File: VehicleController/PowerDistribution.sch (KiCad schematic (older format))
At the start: 20 parts, among them U10 BTS6133D, U11 R-78E5.0-1.0, U9 TL431

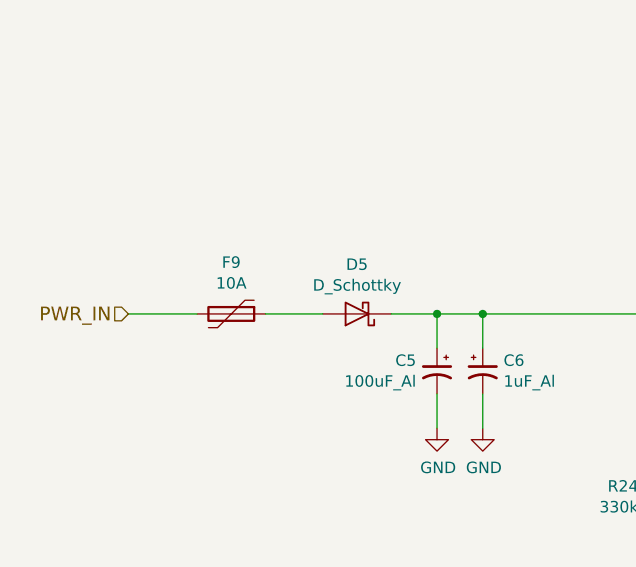
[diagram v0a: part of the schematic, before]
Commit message: Re-do MX120, GDS->GSD, Associations.
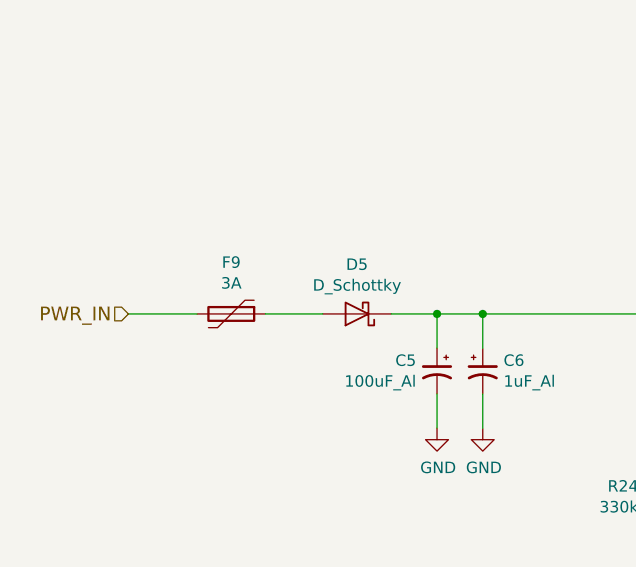
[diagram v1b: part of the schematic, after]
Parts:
- C6: footprint Capacitors_SMD:c_elec_4x4.5 -> Capacitors_SMD:C_0805_HandSoldering
- D5, D6: footprint Diodes_SMD:SMA_Handsoldering -> Diodes_SMD:D_SMC_Handsoldering
- D7: footprint (none) -> Diodes_SMD:D_SOD-323_HandSoldering
- F10: footprint Fuse_Holders_and_Fuses:Fuse_SMD1206_HandSoldering -> Resistors_SMD:R_1210_HandSoldering
- F9: value 10A -> 3A; footprint (none) -> Resistors_SMD:R_1210_HandSoldering
- U10: footprint UNCAMotorsports:TO-252-5 -> UNCA Motorsports:TO-252-5
- U11: footprint UNCAMotorsports:R-78Cxx-1.0 -> UNCA Motorsports:R-78Cxx-1.0
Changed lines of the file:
@@
 F 0 "D5" H 3000 2534 50  0000 C CNN
 F 1 "D_Schottky" H 3000 2625 50  0000 C CNN
-F 2 "Diodes_SMD:SMA_Handsoldering" H 3000 2750 50  0001 C CNN
+F 2 "Diodes_SMD:D_SMC_Handsoldering" H 3000 2750 50  0001 C CNN
 F 3 "" H 3000 2750 50  0000 C CNN
 	1    3000 2750
@@
 P 2450 2750
 F 0 "F9" V 2225 2750 50  0000 C CNN
-F 1 "10A" V 2316 2750 50  0000 C CNN
-F 2 "" H 2500 2550 50  0001 L CNN
+F 1 "3A" V 2316 2750 50  0000 C CNN
+F 2 "Resistors_SMD:R_1210_HandSoldering" H 2500 2550 50  0001 L CNN
 F 3 "" H 2450 2750 50  0001 C CNN
 	1    2450 2750
@@
 F 0 "U10" H 6550 3237 60  0000 C CNN
 F 1 "BTS6133D" H 6550 3131 60  0000 C CNN
-F 2 "UNCAMotorsports:TO-252-5" H 6700 3050 60  0001 C CNN
+F 2 "UNCA Motorsports:TO-252-5" H 6700 3050 60  0001 C CNN
 F 3 "" H 6700 3050 60  0000 C CNN
 	1    6550 2850
@@
 $EndComp
 $Comp
-L GND #PWR43
+L GND #PWR042
 U 1 1 587C7BE3
 P 5850 3650
-F 0 "#PWR43" H 5850 3400 50  0001 C CNN
+F 0 "#PWR042" H 5850 3400 50  0001 C CNN
 F 1 "GND" H 5855 3477 50  0000 C CNN
 F 2 "" H 5850 3650 50  0000 C CNN
@@
 $EndComp
 $Comp
-L GND #PWR42
+L GND #PWR043
 U 1 1 587C7BF7
 P 4300 4700
-F 0 "#PWR42" H 4300 4450 50  0001 C CNN
+F 0 "#PWR043" H 4300 4450 50  0001 C CNN
 F 1 "GND" H 4305 4527 50  0000 C CNN
 F 2 "" H 4300 4700 50  0000 C CNN
@@
 $EndComp
 $Comp
-L GND #PWR45
+L GND #PWR044
 U 1 1 58AEB860
 P 8650 3250
-F 0 "#PWR45" H 8650 3000 50  0001 C CNN
+F 0 "#PWR044" H 8650 3000 50  0001 C CNN
 F 1 "GND" H 8655 3077 50  0000 C CNN
 F 2 "" H 8650 3250 50  0000 C CNN
@@
 5V
 $Comp
-L PWR_FLAG #FLG3
+L PWR_FLAG #FLG045
 U 1 1 58AF2028
 P 5550 1000
-F 0 "#FLG3" H 5550 1095 50  0001 C CNN
+F 0 "#FLG045" H 5550 1095 50  0001 C CNN
 F 1 "PWR_FLAG" H 5550 1224 50  0001 C CNN
 F 2 "" H 5550 1000 50  0000 C CNN
@@
 12V
 $Comp
-L GND #PWR40
+L GND #PWR046
 U 1 1 58B0EFE3
 P 3350 3250
-F 0 "#PWR40" H 3350 3000 50  0001 C CNN
+F 0 "#PWR046" H 3350 3000 50  0001 C CNN
 F 1 "GND" H 3355 3077 50  0000 C CNN
 F 2 "" H 3350 3250 50  0000 C CNN
@@
 $EndComp
 $Comp
-L GND #PWR41
+L GND #PWR047
 U 1 1 58B0F09D
 P 3550 3250
-F 0 "#PWR41" H 3550 3000 50  0001 C CNN
+F 0 "#PWR047" H 3550 3000 50  0001 C CNN
 F 1 "GND" H 3555 3077 50  0000 C CNN
 F 2 "" H 3550 3250 50  0000 C CNN
@@
 F 0 "D6" V 5354 3929 50  0000 L CNN
 F 1 "D_ALT" V 5445 3929 50  0000 L CNN
-F 2 "Diodes_SMD:SMA_Handsoldering" H 5400 3850 50  0001 C CNN
+F 2 "Diodes_SMD:D_SMC_Handsoldering" H 5400 3850 50  0001 C CNN
 F 3 "" H 5400 3850 50  0000 C CNN
 	1    5400 3850
@@
 $EndComp
 $Comp
-L +5V #PWR47
+L +5V #PWR048
 U 1 1 58BE7A1A
 P 9300 2600
-F 0 "#PWR47" H 9350 2650 50  0001 C CNN
+F 0 "#PWR048" H 9350 2650 50  0001 C CNN
 F 1 "+5V" H 9315 2773 50  0000 C CNN
 F 2 "" H 550 -100 50  0001 C CNN
@@
 F 0 "F10" V 7625 2750 50  0000 C CNN
 F 1 "1A" V 7716 2750 50  0000 C CNN
-F 2 "Fuse_Holders_and_Fuses:Fuse_SMD1206_HandSoldering" H 7900 2550 50  0001 L CNN
+F 2 "Resistors_SMD:R_1210_HandSoldering" H 7900 2550 50  0001 L CNN
 F 3 "" H 7850 2750 50  0001 C CNN
 	1    7850 2750
@@
 $EndComp
 $Comp
-L GND #PWR44
+L GND #PWR049
 U 1 1 58C31B60
 P 7500 3500
-F 0 "#PWR44" H 7500 3250 50  0001 C CNN
+F 0 "#PWR049" H 7500 3250 50  0001 C CNN
 F 1 "GND" H 7505 3327 50  0000 C CNN
 F 2 "" H 7500 3500 50  0000 C CNN
@@
 $EndComp
 $Comp
-L GND #PWR48
+L GND #PWR050
 U 1 1 58C32364
 P 9650 3500
-F 0 "#PWR48" H 9650 3250 50  0001 C CNN
+F 0 "#PWR050" H 9650 3250 50  0001 C CNN
 F 1 "GND" H 9655 3327 50  0000 C CNN
 F 2 "" H 9650 3500 50  0000 C CNN
@@
 F 0 "C6" H 3641 3046 50  0000 L CNN
 F 1 "1uF_Al" H 3641 2955 50  0000 L CNN
-F 2 "Capacitors_SMD:c_elec_4x4.5" H 900 -350 50  0001 C CNN
+F 2 "Capacitors_SMD:C_0805_HandSoldering" H 900 -350 50  0001 C CNN
 F 3 "" H 900 -350 50  0001 C CNN
 	1    3550 3000
@@
 F 0 "U11" H 8650 3037 60  0000 C CNN
 F 1 "R-78E5.0-1.0" H 8650 2931 60  0000 C CNN
-F 2 "UNCAMotorsports:R-78Cxx-1.0" H 2600 1150 60  0001 C CNN
+F 2 "UNCA Motorsports:R-78Cxx-1.0" H 2600 1150 60  0001 C CNN
 F 3 "" H 2600 1150 60  0000 C CNN
 	1    8650 2750
@@
 F 0 "D7" H 6050 3390 50  0000 C CNN
 F 1 "3.3V" H 6050 3210 50  0000 C CNN
-F 2 "" V 6050 3300 50  0001 C CNN
+F 2 "Diodes_SMD:D_SOD-323_HandSoldering" V 6050 3300 50  0001 C CNN
 F 3 "" V 6050 3300 50  0001 C CNN
 	1    6050 3300

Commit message: Library Fixes
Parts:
- D5, D6: footprint Diodes_SMD:D_SMC_Handsoldering -> Diodes_SMD:SMC_Handsoldering
- D7: footprint Diodes_SMD:D_SOD-323_HandSoldering -> Diodes_SMD:SOD-323
- U10: footprint UNCA Motorsports:TO-252-5 -> UNCAMotorsports:TO-252-5
- U11: footprint UNCA Motorsports:R-78Cxx-1.0 -> UNCAMotorsports:R-78Cxx-1.0
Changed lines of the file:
@@
 F 0 "D5" H 3000 2534 50  0000 C CNN
 F 1 "D_Schottky" H 3000 2625 50  0000 C CNN
-F 2 "Diodes_SMD:D_SMC_Handsoldering" H 3000 2750 50  0001 C CNN
+F 2 "Diodes_SMD:SMC_Handsoldering" H 3000 2750 50  0001 C CNN
 F 3 "" H 3000 2750 50  0000 C CNN
 	1    3000 2750
@@
 F 0 "U10" H 6550 3237 60  0000 C CNN
 F 1 "BTS6133D" H 6550 3131 60  0000 C CNN
-F 2 "UNCA Motorsports:TO-252-5" H 6700 3050 60  0001 C CNN
+F 2 "UNCAMotorsports:TO-252-5" H 6700 3050 60  0001 C CNN
 F 3 "" H 6700 3050 60  0000 C CNN
 	1    6550 2850
@@
 F 0 "D6" V 5354 3929 50  0000 L CNN
 F 1 "D_ALT" V 5445 3929 50  0000 L CNN
-F 2 "Diodes_SMD:D_SMC_Handsoldering" H 5400 3850 50  0001 C CNN
+F 2 "Diodes_SMD:SMC_Handsoldering" H 5400 3850 50  0001 C CNN
 F 3 "" H 5400 3850 50  0000 C CNN
 	1    5400 3850
@@
 F 0 "U11" H 8650 3037 60  0000 C CNN
 F 1 "R-78E5.0-1.0" H 8650 2931 60  0000 C CNN
-F 2 "UNCA Motorsports:R-78Cxx-1.0" H 2600 1150 60  0001 C CNN
+F 2 "UNCAMotorsports:R-78Cxx-1.0" H 2600 1150 60  0001 C CNN
 F 3 "" H 2600 1150 60  0000 C CNN
 	1    8650 2750
@@
 F 0 "D7" H 6050 3390 50  0000 C CNN
 F 1 "3.3V" H 6050 3210 50  0000 C CNN
-F 2 "Diodes_SMD:D_SOD-323_HandSoldering" V 6050 3300 50  0001 C CNN
+F 2 "Diodes_SMD:SOD-323" V 6050 3300 50  0001 C CNN
 F 3 "" V 6050 3300 50  0001 C CNN
 	1    6050 3300

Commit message: Small schematic fixes, start layout
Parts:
- D5, D6: footprint Diodes_SMD:SMC_Handsoldering -> Diodes_SMD:SMA_Handsoldering
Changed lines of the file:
@@
 LIBS:VehicleController-rescue
 LIBS:UNCAMotorsports
-LIBS:power
-LIBS:device
-LIBS:transistors
-LIBS:conn
-LIBS:linear
-LIBS:regul
-LIBS:74xx
-LIBS:cmos4000
-LIBS:adc-dac
-LIBS:memory
-LIBS:xilinx
-LIBS:microcontrollers
-LIBS:dsp
-LIBS:microchip
-LIBS:analog_switches
-LIBS:motorola
-LIBS:texas
-LIBS:intel
-LIBS:audio
-LIBS:interface
-LIBS:digital-audio
-LIBS:philips
-LIBS:display
-LIBS:cypress
-LIBS:siliconi
-LIBS:opto
-LIBS:atmel
-LIBS:contrib
-LIBS:valves
 LIBS:Common-Parts-Library-CPL
 LIBS:relays
 LIBS:SystemBlocks
-LIBS:dc-dc
-LIBS:Power_Management
-LIBS:switches
 LIBS:VehicleController-cache
-EELAYER 25 0
+EELAYER 26 0
 EELAYER END
 $Descr A4 11693 8268
@@
 F 0 "D5" H 3000 2534 50  0000 C CNN
 F 1 "D_Schottky" H 3000 2625 50  0000 C CNN
-F 2 "Diodes_SMD:SMC_Handsoldering" H 3000 2750 50  0001 C CNN
+F 2 "Diodes_SMD:SMA_Handsoldering" H 3000 2750 50  0001 C CNN
 F 3 "" H 3000 2750 50  0000 C CNN
 	1    3000 2750
@@
 F 0 "D6" V 5354 3929 50  0000 L CNN
 F 1 "D_ALT" V 5445 3929 50  0000 L CNN
-F 2 "Diodes_SMD:SMC_Handsoldering" H 5400 3850 50  0001 C CNN
+F 2 "Diodes_SMD:SMA_Handsoldering" H 5400 3850 50  0001 C CNN
 F 3 "" H 5400 3850 50  0000 C CNN
 	1    5400 3850

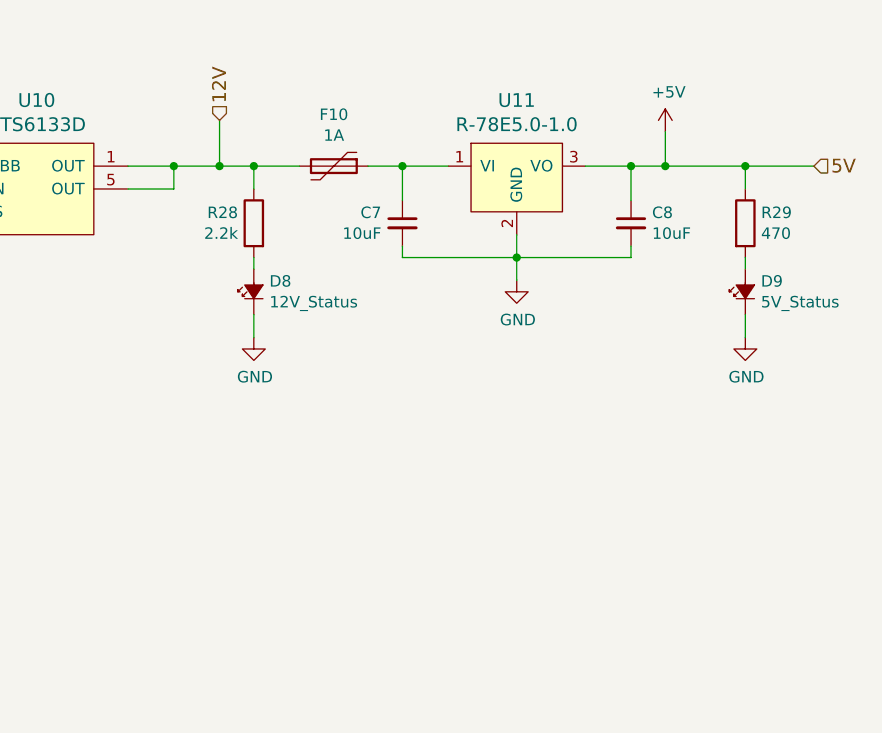
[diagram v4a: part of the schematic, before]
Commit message: 2x10 connector is now a nanofit, VCU
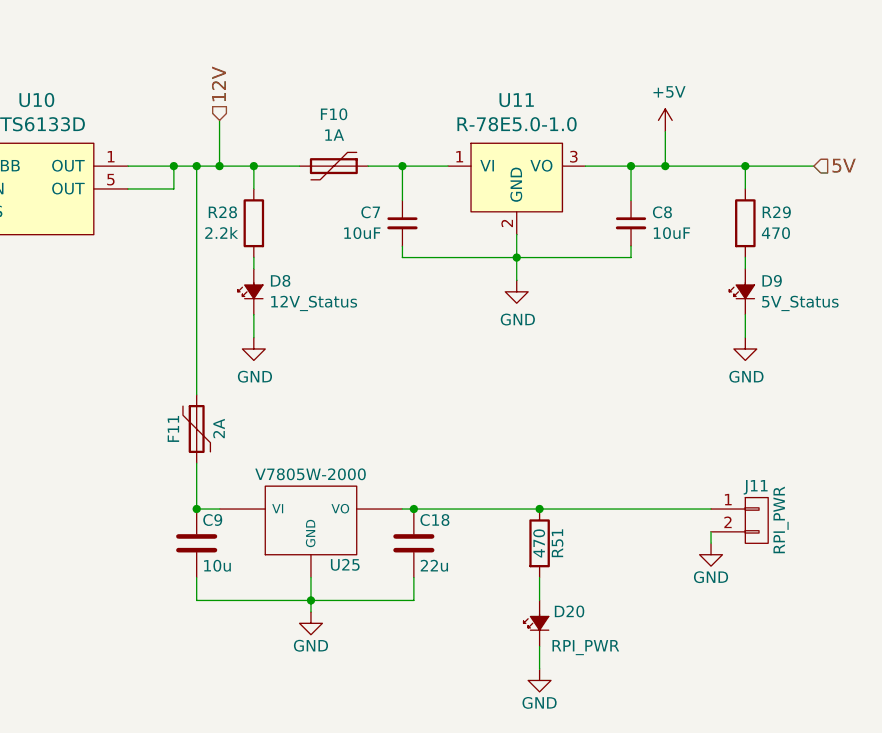
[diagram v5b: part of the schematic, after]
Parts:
- added C18: 22u, Capacitors_SMD:C_0805_HandSoldering, symbol C
- added C9: 10u, Capacitors_SMD:C_0805_HandSoldering, symbol C
- added D20: RPI_PWR, LEDs:LED_0805, symbol LED_Small_ALT
- added F11: 2A, Resistors_SMD:R_1210_HandSoldering, symbol Polyfuse
- added J11: RPI_PWR, Connectors_Molex:Molex_NanoFit_1x02x2.50mm_Straight, symbol CONN_01X02
- added R51: 470, Resistors_SMD:R_0805_HandSoldering, symbol R
- added U25: V7805W-2000, UNCAMotorsports:R-78Cxx-1.0, symbol V7805W-500
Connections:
- net 12V: now also F11.1
- net GND: now also C18.2, C9.2, D20.1 (K), J11.2 (P2), U25.2 (GND)
- new net: C9.1, F11.2, U25.1 (VI)
- new net: C18.1, J11.1 (P1), R51.1, U25.3 (VO)
- new net: D20.2 (A), R51.2
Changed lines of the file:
@@
 Wire Wire Line
 	6050 3550 5850 3550
+$Comp
+L V7805W-500 U25
+U 1 1 5930FD3A
+P 7750 4300
+F 0 "U25" H 7900 4104 50  0000 C CNN
+F 1 "V7805W-2000" H 7750 4500 50  0000 C CNN
+F 2 "UNCAMotorsports:R-78Cxx-1.0" H 7750 4300 50  0001 C CNN
+F 3 "" H 7750 4300 50  0000 C CNN
+	1    7750 4300
+	1    0    0    -1
+$EndComp
+Wire Wire Line
+	7250 4250 7350 4250
+Connection ~ 7250 2750
+$Comp
+L GND #PWR051
+U 1 1 5930FE1B
+P 7750 4700
+F 0 "#PWR051" H 7750 4450 50  0001 C CNN
+F 1 "GND" H 7750 4550 50  0000 C CNN
+F 2 "" H 7750 4700 50  0001 C CNN
+F 3 "" H 7750 4700 50  0001 C CNN
+	1    7750 4700
+	1    0    0    -1
+$EndComp
+Wire Wire Line
+	7750 4700 7750 4550
+$Comp
+L C C9
+U 1 1 5930FEB3
+P 7250 4400
+F 0 "C9" H 7275 4500 50  0000 L CNN
+F 1 "10u" H 7275 4300 50  0000 L CNN
+F 2 "Capacitors_SMD:C_0805_HandSoldering" H 7288 4250 50  0001 C CNN
+F 3 "" H 7250 4400 50  0001 C CNN
+	1    7250 4400
+	1    0    0    -1
+$EndComp
+$Comp
+L C C18
+U 1 1 5930FF1A
+P 8200 4400
+F 0 "C18" H 8225 4500 50  0000 L CNN
+F 1 "22u" H 8225 4300 50  0000 L CNN
+F 2 "Capacitors_SMD:C_0805_HandSoldering" H 8238 4250 50  0001 C CNN
+F 3 "" H 8200 4400 50  0001 C CNN
+	1    8200 4400
+	1    0    0    -1
+$EndComp
+Wire Wire Line
+	8150 4250 9500 4250
+Wire Wire Line
+	7250 4550 7250 4650
+Wire Wire Line
+	7250 4650 8200 4650
+Connection ~ 7750 4650
+Wire Wire Line
+	8200 4650 8200 4550
+Connection ~ 7250 4250
+Connection ~ 8200 4250
+$Comp
+L R R51
+U 1 1 59310885
+P 8750 4400
+F 0 "R51" V 8830 4400 50  0000 C CNN
+F 1 "470" V 8750 4400 50  0000 C CNN
+F 2 "Resistors_SMD:R_0805_HandSoldering" V 8680 4400 50  0001 C CNN
+F 3 "" H 8750 4400 50  0001 C CNN
+	1    8750 4400
+	1    0    0    -1
+$EndComp
+Wire Wire Line
+	8750 4550 8750 4650
+$Comp
+L GND #PWR052
+U 1 1 593109F8
+P 8750 4950
+F 0 "#PWR052" H 8750 4700 50  0001 C CNN
+F 1 "GND" H 8750 4800 50  0000 C CNN
+F 2 "" H 8750 4950 50  0001 C CNN
+F 3 "" H 8750 4950 50  0001 C CNN
+	1    8750 4950
+	1    0    0    -1
+$EndComp
+Wire Wire Line
+	8750 4850 8750 4950
+$Comp
+L CONN_01X02 J11
+U 1 1 59310B7F
+P 9700 4300
+F 0 "J11" H 9700 4450 50  0000 C CNN
+F 1 "RPI_PWR" V 9800 4300 50  0000 C CNN
+F 2 "Connectors_Molex:Molex_NanoFit_1x02x2.50mm_Straight" H 9700 4300 50  0001 C CNN
+F 3 "" H 9700 4300 50  0001 C CNN
+	1    9700 4300
+	1    0    0    -1
+$EndComp
+Connection ~ 8750 4250
+$Comp
+L GND #PWR053
+U 1 1 59310C3E
+P 9500 4400
+F 0 "#PWR053" H 9500 4150 50  0001 C CNN
+F 1 "GND" H 9500 4250 50  0000 C CNN
+F 2 "" H 9500 4400 50  0001 C CNN
+F 3 "" H 9500 4400 50  0001 C CNN
+	1    9500 4400
+	1    0    0    -1
+$EndComp
+Wire Wire Line
+	9500 4400 9500 4350
+$Comp
+L LED_Small_ALT D20
+U 1 1 59310E6C
+P 8750 4750
+F 0 "D20" V 8800 4550 50  0000 L CNN
+F 1 "RPI_PWR" V 8650 4400 50  0000 L CNN
+F 2 "LEDs:LED_0805" V 8750 4750 50  0001 C CNN
+F 3 "" V 8750 4750 50  0001 C CNN
+	1    8750 4750
+	0    -1   -1   0
+$EndComp
+Wire Wire Line
+	7250 3750 7250 2750
+Wire Wire Line
+	7250 4050 7250 4250
+$Comp
+L Polyfuse F11
+U 1 1 59311313
+P 7250 3900
+F 0 "F11" V 7150 3900 50  0000 C CNN
+F 1 "2A" V 7350 3900 50  0000 C CNN
+F 2 "Resistors_SMD:R_1210_HandSoldering" H 7300 3700 50  0001 L CNN
+F 3 "" H 7250 3900 50  0001 C CNN
+	1    7250 3900
+	1    0    0    -1
+$EndComp
 $EndSCHEMATC

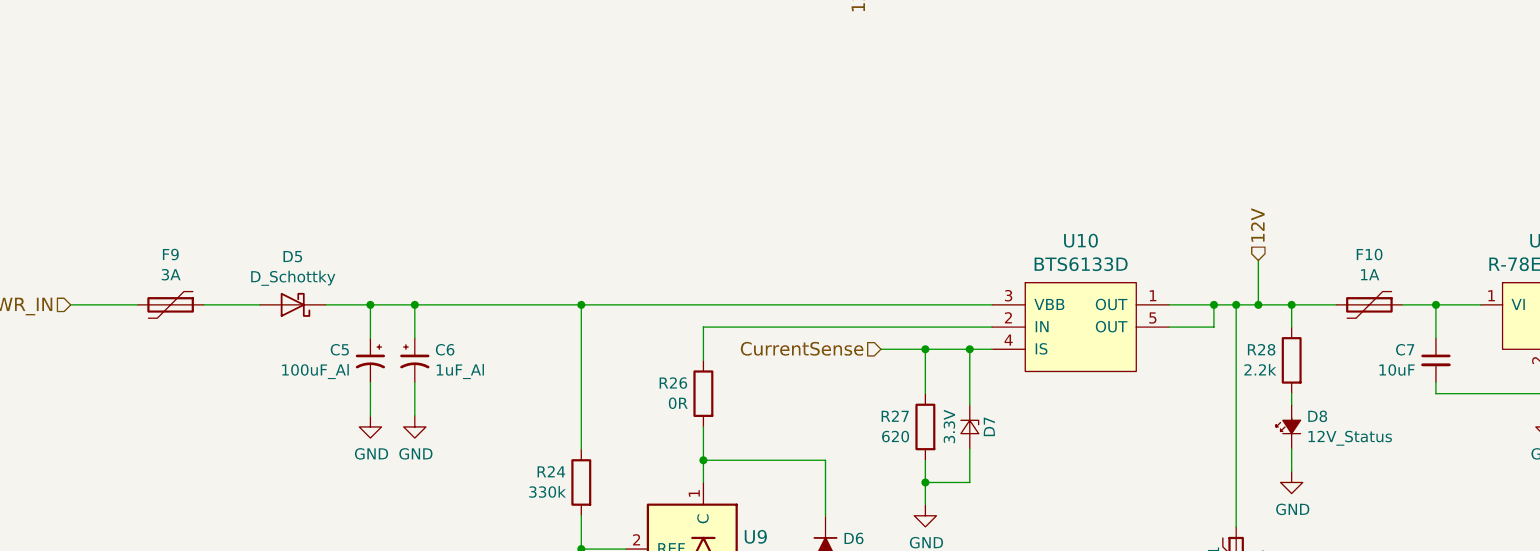
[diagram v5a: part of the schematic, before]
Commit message: Major VCU Layout changes
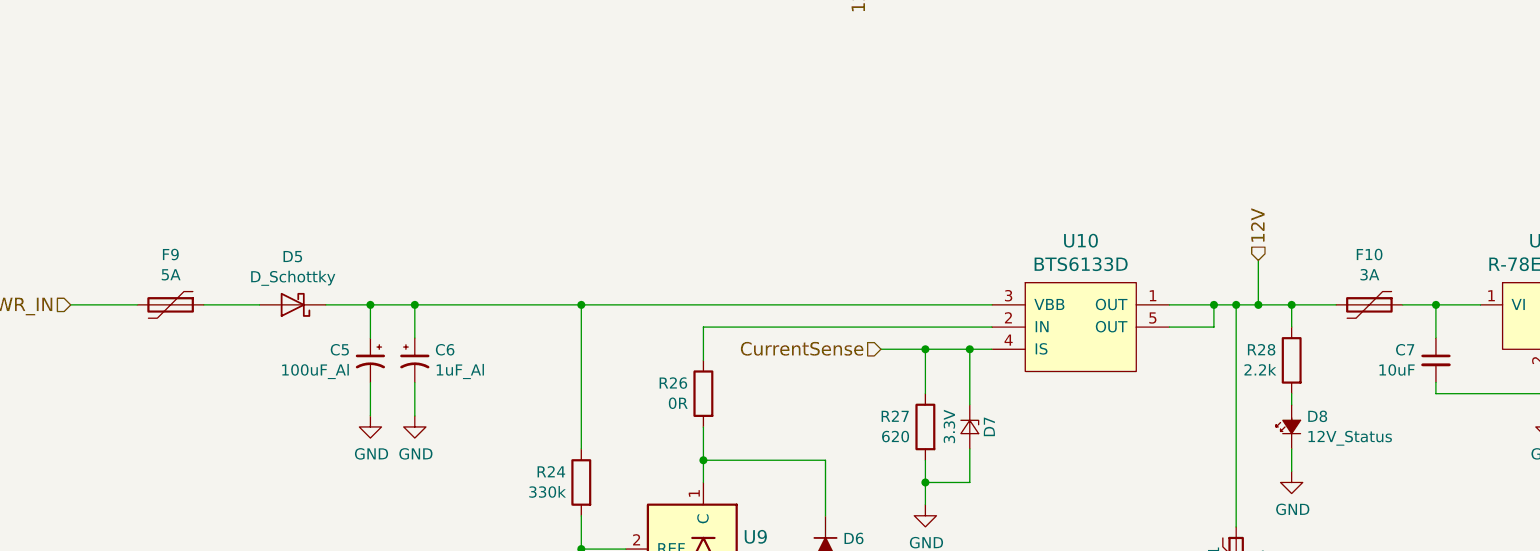
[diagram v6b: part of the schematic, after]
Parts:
- F10: value 1A -> 3A
- F9: value 3A -> 5A
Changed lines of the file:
@@
 P 2450 2750
 F 0 "F9" V 2225 2750 50  0000 C CNN
-F 1 "3A" V 2316 2750 50  0000 C CNN
+F 1 "5A" V 2316 2750 50  0000 C CNN
 F 2 "Resistors_SMD:R_1210_HandSoldering" H 2500 2550 50  0001 L CNN
 F 3 "" H 2450 2750 50  0001 C CNN
@@
 $EndComp
 $Comp
-L GND #PWR042
+L GND #PWR041
 U 1 1 587C7BE3
 P 5850 3650
-F 0 "#PWR042" H 5850 3400 50  0001 C CNN
+F 0 "#PWR041" H 5850 3400 50  0001 C CNN
 F 1 "GND" H 5855 3477 50  0000 C CNN
 F 2 "" H 5850 3650 50  0000 C CNN
@@
 $EndComp
 $Comp
-L GND #PWR043
+L GND #PWR042
 U 1 1 587C7BF7
 P 4300 4700
-F 0 "#PWR043" H 4300 4450 50  0001 C CNN
+F 0 "#PWR042" H 4300 4450 50  0001 C CNN
 F 1 "GND" H 4305 4527 50  0000 C CNN
 F 2 "" H 4300 4700 50  0000 C CNN
@@
 $EndComp
 $Comp
-L GND #PWR044
+L GND #PWR043
 U 1 1 58AEB860
 P 8650 3250
-F 0 "#PWR044" H 8650 3000 50  0001 C CNN
+F 0 "#PWR043" H 8650 3000 50  0001 C CNN
 F 1 "GND" H 8655 3077 50  0000 C CNN
 F 2 "" H 8650 3250 50  0000 C CNN
@@
 5V
 $Comp
-L PWR_FLAG #FLG045
+L PWR_FLAG #FLG044
 U 1 1 58AF2028
 P 5550 1000
-F 0 "#FLG045" H 5550 1095 50  0001 C CNN
+F 0 "#FLG044" H 5550 1095 50  0001 C CNN
 F 1 "PWR_FLAG" H 5550 1224 50  0001 C CNN
 F 2 "" H 5550 1000 50  0000 C CNN
@@
 12V
 $Comp
-L GND #PWR046
+L GND #PWR045
 U 1 1 58B0EFE3
 P 3350 3250
-F 0 "#PWR046" H 3350 3000 50  0001 C CNN
+F 0 "#PWR045" H 3350 3000 50  0001 C CNN
 F 1 "GND" H 3355 3077 50  0000 C CNN
 F 2 "" H 3350 3250 50  0000 C CNN
@@
 $EndComp
 $Comp
-L GND #PWR047
+L GND #PWR046
 U 1 1 58B0F09D
 P 3550 3250
-F 0 "#PWR047" H 3550 3000 50  0001 C CNN
+F 0 "#PWR046" H 3550 3000 50  0001 C CNN
 F 1 "GND" H 3555 3077 50  0000 C CNN
 F 2 "" H 3550 3250 50  0000 C CNN
@@
 $EndComp
 $Comp
-L +5V #PWR048
+L +5V #PWR047
 U 1 1 58BE7A1A
 P 9300 2600
-F 0 "#PWR048" H 9350 2650 50  0001 C CNN
+F 0 "#PWR047" H 9350 2650 50  0001 C CNN
 F 1 "+5V" H 9315 2773 50  0000 C CNN
 F 2 "" H 550 -100 50  0001 C CNN
@@
 P 7850 2750
 F 0 "F10" V 7625 2750 50  0000 C CNN
-F 1 "1A" V 7716 2750 50  0000 C CNN
+F 1 "3A" V 7716 2750 50  0000 C CNN
 F 2 "Resistors_SMD:R_1210_HandSoldering" H 7900 2550 50  0001 L CNN
 F 3 "" H 7850 2750 50  0001 C CNN
@@
 $EndComp
 $Comp
-L GND #PWR049
+L GND #PWR048
 U 1 1 58C31B60
 P 7500 3500
-F 0 "#PWR049" H 7500 3250 50  0001 C CNN
+F 0 "#PWR048" H 7500 3250 50  0001 C CNN
 F 1 "GND" H 7505 3327 50  0000 C CNN
 F 2 "" H 7500 3500 50  0000 C CNN
@@
 $EndComp
 $Comp
-L GND #PWR050
+L GND #PWR049
 U 1 1 58C32364
 P 9650 3500
-F 0 "#PWR050" H 9650 3250 50  0001 C CNN
+F 0 "#PWR049" H 9650 3250 50  0001 C CNN
 F 1 "GND" H 9655 3327 50  0000 C CNN
 F 2 "" H 9650 3500 50  0000 C CNN
@@
 Connection ~ 7250 2750
 $Comp
-L GND #PWR051
+L GND #PWR050
 U 1 1 5930FE1B
 P 7750 4700
-F 0 "#PWR051" H 7750 4450 50  0001 C CNN
+F 0 "#PWR050" H 7750 4450 50  0001 C CNN
 F 1 "GND" H 7750 4550 50  0000 C CNN
 F 2 "" H 7750 4700 50  0001 C CNN
@@
 	8750 4550 8750 4650
 $Comp
-L GND #PWR052
+L GND #PWR051
 U 1 1 593109F8
 P 8750 4950
-F 0 "#PWR052" H 8750 4700 50  0001 C CNN
+F 0 "#PWR051" H 8750 4700 50  0001 C CNN
 F 1 "GND" H 8750 4800 50  0000 C CNN
 F 2 "" H 8750 4950 50  0001 C CNN
@@
 Connection ~ 8750 4250
 $Comp
-L GND #PWR053
+L GND #PWR052
 U 1 1 59310C3E
 P 9500 4400
-F 0 "#PWR053" H 9500 4150 50  0001 C CNN
+F 0 "#PWR052" H 9500 4150 50  0001 C CNN
 F 1 "GND" H 9500 4250 50  0000 C CNN
 F 2 "" H 9500 4400 50  0001 C CNN
